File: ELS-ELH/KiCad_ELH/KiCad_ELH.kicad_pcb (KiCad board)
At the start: 2 copper layers, 248.6 x 89.7 mm, 62 parts, among them J10 COM CTR-MAIN, J2 MOSFETS MAIN, J3 MOSFETS MAIN, J4 Pressure Transducer, J5 COM CTR-MAIN, J6 Sensors, J7 Sensors, J9 Pressure Transducer, Q1 IRLZ44N, Q2 IRLZ44N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

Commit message: Components preliminar distribution
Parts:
- removed Bornera1: Sensor Power Supply Screw Terminal, ELH_Library:Bornera 2P
- removed J10, J5: COM CTR-MAIN, ELH_Library:2Pin Header
- removed J3: MOSFETS MAIN, ELH_Library:2Pin Header
- removed J4, J9: Pressure Transducer, ELH_Library:3Pin Header
- removed J6, J7: Sensors, ELH_Library:2Pin Header
- added Bornera2: Camera Screw Terminal, ELH_Library:Bornera 2P, F.Cu at (92.0, -20.9)
- added J1: Pressure Transducer Screw Terminal, TerminalBlock:TerminalBlock_MaiXu_MX126-5.0-03P_1x03_P5.00mm, F.Cu at (123.6, 40.1)
- added J11: Conn_01x09_Socket, Connector_Hirose:Hirose_DF13-09P-1.25DSA_1x09_P1.25mm_Vertical, F.Cu at (22.2, -40.3)
- added J8: RW1 Screw Terminal, TerminalBlock:TerminalBlock_MaiXu_MX126-5.0-04P_1x04_P5.00mm, F.Cu at (156.7, 39.9)
- Adapter1, IMU1: moved to B.Cu
- Bornera3: value Camera Screw Terminal -> Actuator Power Supply Screw Terminal
- Bornera6: value Actuator Power Supply Screw Terminal -> Sensor Power Supply Screw Terminal
- J2: value MOSFETS MAIN -> Conn_01x09_Pin; footprint ELH_Library:2Pin Header -> Connector_Hirose:Hirose_DF13-09P-1.25DSA_1x09_P1.25mm_Vertical
- moved J2 224.5 mm to (149.3, -39.6), turned to 0 degrees
- moved C1 115.7 mm to (121.2, -34.5), turned to 90 degrees
- moved C3 105.1 mm to (127.7, -38.2), turned to -90 degrees
- moved D9 100.0 mm to (158.8, -24.8), turned to -90 degrees
- moved Bornera6 95.6 mm to (108.0, 36.2)
- moved ADC1 88.1 mm to (-2.49, -41.6)
- moved D3 85.6 mm to (110.6, -2.22)
- moved W25QXX1 82.5 mm to (15.0, -8.71)
- moved SD_Adapter1 81.4 mm to (20.0, -34.2)
- moved Adapter1 75.5 mm to (15.5, 19.8), turned to 180 degrees
- moved Bornera5 74.1 mm to (161.8, -25.5), turned to 90 degrees
- moved BME2 71.3 mm to (40.8, 10.1), turned to -90 degrees
- moved R9 69.3 mm to (102.8, 41.1)
- moved C10 66.4 mm to (159.1, 15.1), turned to 180 degrees
- moved R1 64.0 mm to (109.6, 11.1)
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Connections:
- Bornera3 pad 1: Net-(Bornera3-Pin_1) -> Net-(Bornera3-Pin_2)
- Bornera3 pad 2: Net-(Bornera3-Pin_2) -> Net-(Bornera3-Pin_1)
- Bornera6 pad 1: Net-(Bornera6-Pin_1) -> Net-(BOOST1-IN+)
- Bornera6 pad 2: Net-(Bornera6-Pin_2) -> Net-(BOOST1-IN-)
- Driver_DC2 pad 6: Net-(Driver_DC2-B02) -> unconnected-(Driver_DC2-B02-Pad6)
- Driver_DC2 pad 7: Net-(Driver_DC2-B01) -> unconnected-(Driver_DC2-B01-Pad7)
- J2 pad 1: /sensors/MOS1_2 -> /MOS1_1
- J2 pad 2: /sensors/MOS2_2 -> /MOS2_1
- Regulator3 pad 3: Net-(Bornera3-Pin_1) -> Net-(Bornera2-Pin_1)
- Regulator3 pad 4: Net-(Bornera3-Pin_2) -> Net-(Bornera2-Pin_2)
- Regulator4 pad 1: Net-(Bornera6-Pin_2) -> Net-(Bornera3-Pin_2)
- Regulator4 pad 2: Net-(Bornera6-Pin_1) -> Net-(Bornera3-Pin_1)
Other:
- board size 248.6 x 89.7 mm -> 216.1 x 89.7 mm
- board text added: "Screw Terminal"

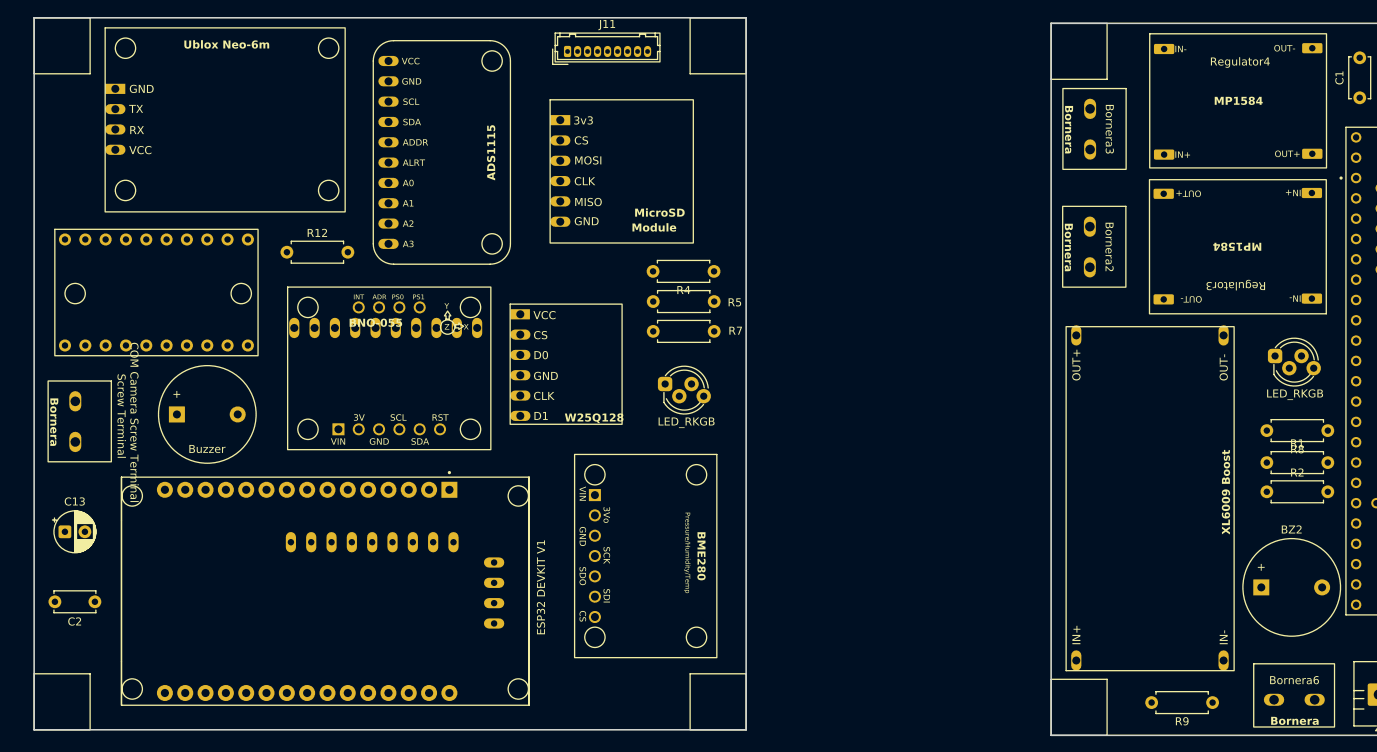
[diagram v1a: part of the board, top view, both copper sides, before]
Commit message: Editing some footprints and connections
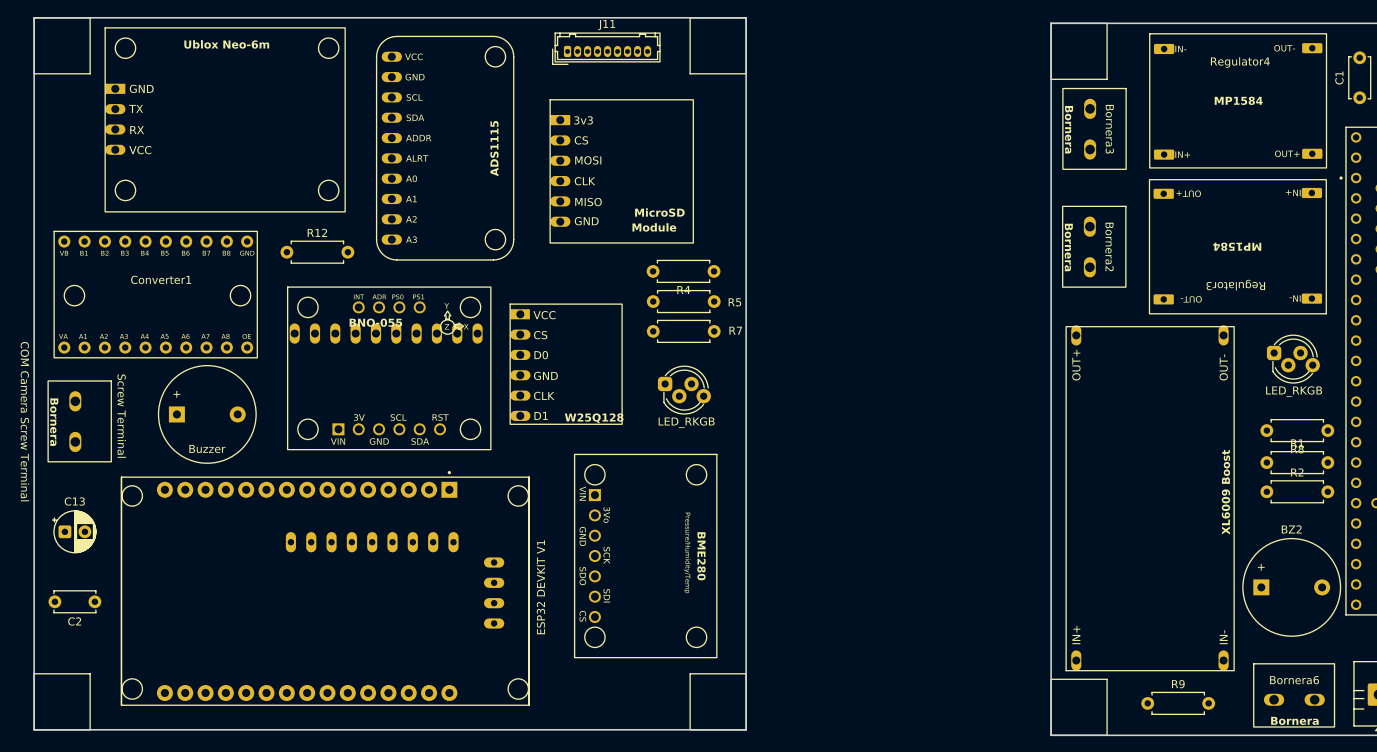
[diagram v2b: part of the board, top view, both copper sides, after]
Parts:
- moved R9 8.11 mm to (94.7, 41.2), turned to 0 degrees
- moved IMU1 0.70 mm to (-13.2, -6.30)
- moved ADC1 0.67 mm to (-2.08, -42.2)
- moved D3 0.40 mm to (110.5, -2.60)
- moved Converter1 0.28 mm to (-42.0, -17.8)
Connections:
- Adapter1 pad 1: unconnected-(Adapter1-VCC-Pad1) -> +5VA
- Adapter1 pad 2: unconnected-(Adapter1-GND-Pad2) -> GND1
- BZ2 pad 2: GND1 -> GND
- Converter1 pad 1: unconnected-(Converter1-VB-Pad1) -> +5VA
- Converter1 pad 10: unconnected-(Converter1-GND-Pad10) -> GND
- Converter1 pad 11: unconnected-(Converter1-VA-Pad11) -> +3.3V
- Converter1 pad 20: unconnected-(Converter1-OE-Pad20) -> +3.3V
- D3 pad 2: GND1 -> GND
